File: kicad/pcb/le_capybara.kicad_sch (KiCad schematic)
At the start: 48 parts, among them J1 USB_C sink board 1.6mm, J2 OLED I2C, U2 STM32F072CBT6, U3 PRTR5V0U2X

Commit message: rerouted pcb
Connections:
- net APLEX_EN1: now also U2.3 (PC14); no longer U2.25 (PB12)
- net ROW0: now also U2.13 (PA3); no longer U2.18 (PB0)
- net ROW1: now also U2.15 (PA5); no longer U2.19 (PB1)
- net ROW2: now also U2.17 (PA7); no longer U2.20 (PB2)
- net ROW3: now also U2.19 (PB1); no longer U2.21 (PB10)
- no-connect marks 21 -> 18
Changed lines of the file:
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@@
   (no_connect (at 59.055 52.07))
   (no_connect (at 26.035 87.63))
-  (no_connect (at 59.055 44.45))
   (no_connect (at 26.035 54.61))
-  (no_connect (at 59.055 54.61))
+  (no_connect (at 26.035 95.25))
   (no_connect (at 59.055 59.69))
-  (no_connect (at 26.035 57.15))
-  (no_connect (at 59.055 49.53))
   (no_connect (at 60.325 69.85))
   (no_connect (at 59.055 36.83))
@@
     )
   )
+  (global_label "ROW1" (shape input) (at 59.055 49.53 0) (fields_autoplaced)
+    (effects (font (size 1.27 1.27)) (justify left))
+    (property "Intersheetrefs" "${INTERSHEET_REFS}" (at 67.2222 49.53 0)
+      (effects (font (size 1.27 1.27)) (justify left) hide)
+    )
+  )
   (global_label "BOOT0" (shape input) (at 83.82 83.82 0) (fields_autoplaced)
     (effects (font (size 1.27 1.27)) (justify left))
@@
     )
   )
-  (global_label "ROW2" (shape input) (at 26.035 69.85 180) (fields_autoplaced)
-    (effects (font (size 1.27 1.27)) (justify right))
-    (property "Intersheetrefs" "${INTERSHEET_REFS}" (at 17.8678 69.85 0)
+  (global_label "ROW3" (shape input) (at 26.035 67.31 180) (fields_autoplaced)
+    (effects (font (size 1.27 1.27)) (justify right))
+    (property "Intersheetrefs" "${INTERSHEET_REFS}" (at 17.8678 67.31 0)
       (effects (font (size 1.27 1.27)) (justify right) hide)
     )
@@
     )
   )
-  (global_label "ROW1" (shape input) (at 26.035 67.31 180) (fields_autoplaced)
-    (effects (font (size 1.27 1.27)) (justify right))
-    (property "Intersheetrefs" "${INTERSHEET_REFS}" (at 17.8678 67.31 0)
-      (effects (font (size 1.27 1.27)) (justify right) hide)
+  (global_label "ROW2" (shape input) (at 59.055 54.61 0) (fields_autoplaced)
+    (effects (font (size 1.27 1.27)) (justify left))
+    (property "Intersheetrefs" "${INTERSHEET_REFS}" (at 67.2222 54.61 0)
+      (effects (font (size 1.27 1.27)) (justify left) hide)
     )
   )
@@
     )
   )
-  (global_label "APLEX_EN1" (shape input) (at 26.035 95.25 180) (fields_autoplaced)
-    (effects (font (size 1.27 1.27)) (justify right))
-    (property "Intersheetrefs" "${INTERSHEET_REFS}" (at 12.7274 95.25 0)
-      (effects (font (size 1.27 1.27)) (justify right) hide)
-    )
-  )
-  (global_label "ROW0" (shape input) (at 26.035 64.77 180) (fields_autoplaced)
-    (effects (font (size 1.27 1.27)) (justify right))
-    (property "Intersheetrefs" "${INTERSHEET_REFS}" (at 17.8678 64.77 0)
-      (effects (font (size 1.27 1.27)) (justify right) hide)
+  (global_label "APLEX_EN1" (shape input) (at 26.035 57.15 180) (fields_autoplaced)
+    (effects (font (size 1.27 1.27)) (justify right))
+    (property "Intersheetrefs" "${INTERSHEET_REFS}" (at 12.7274 57.15 0)
+      (effects (font (size 1.27 1.27)) (justify right) hide)
+    )
+  )
+  (global_label "ROW0" (shape input) (at 59.055 44.45 0) (fields_autoplaced)
+    (effects (font (size 1.27 1.27)) (justify left))
+    (property "Intersheetrefs" "${INTERSHEET_REFS}" (at 67.2222 44.45 0)
+      (effects (font (size 1.27 1.27)) (justify left) hide)
     )
   )
@@
       (effects (font (size 1.27 1.27)) (justify right) hide)
     )
-  )
-  (global_label "ROW3" (shape input) (at 26.035 90.17 180) (fields_autoplaced)
-    (effects (font (size 1.27 1.27)) (justify right))
-    (property "Intersheetrefs" "${INTERSHEET_REFS}" (at 17.8678 90.17 0)
-      (effects (font (size 1.27 1.27)) (justify right) hide)
-    )

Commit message: getting ready for prototype
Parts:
- removed H1, H10, H11, H12, H13, H14, H15, H16, H17, H18, H19, H2, H20, H21, H22, H23, H24, H3, H4, H5, H6, H7, H8, H9: MountingHole, MountingHole:MountingHole_2.2mm_M2_DIN965, symbol Mechanical:MountingHole
- J1: value USB_C sink board 1.6mm -> USB_C sink board 1.3mm; LCSC C2936201 -> C3019717
- SW?: footprint modified_footrprints:SW_SPST_SKQG_WithoutStem -> modified_footprints:SW_SPST_SKQG_WithoutStem
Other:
- added sheet mounting_holes (mounting_holes.kicad_sch)

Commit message: getting ready for prototype
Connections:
- no-connect marks 18 -> 21
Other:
- moved on the sheet: C11, C8, C?, R?, SW?, U2

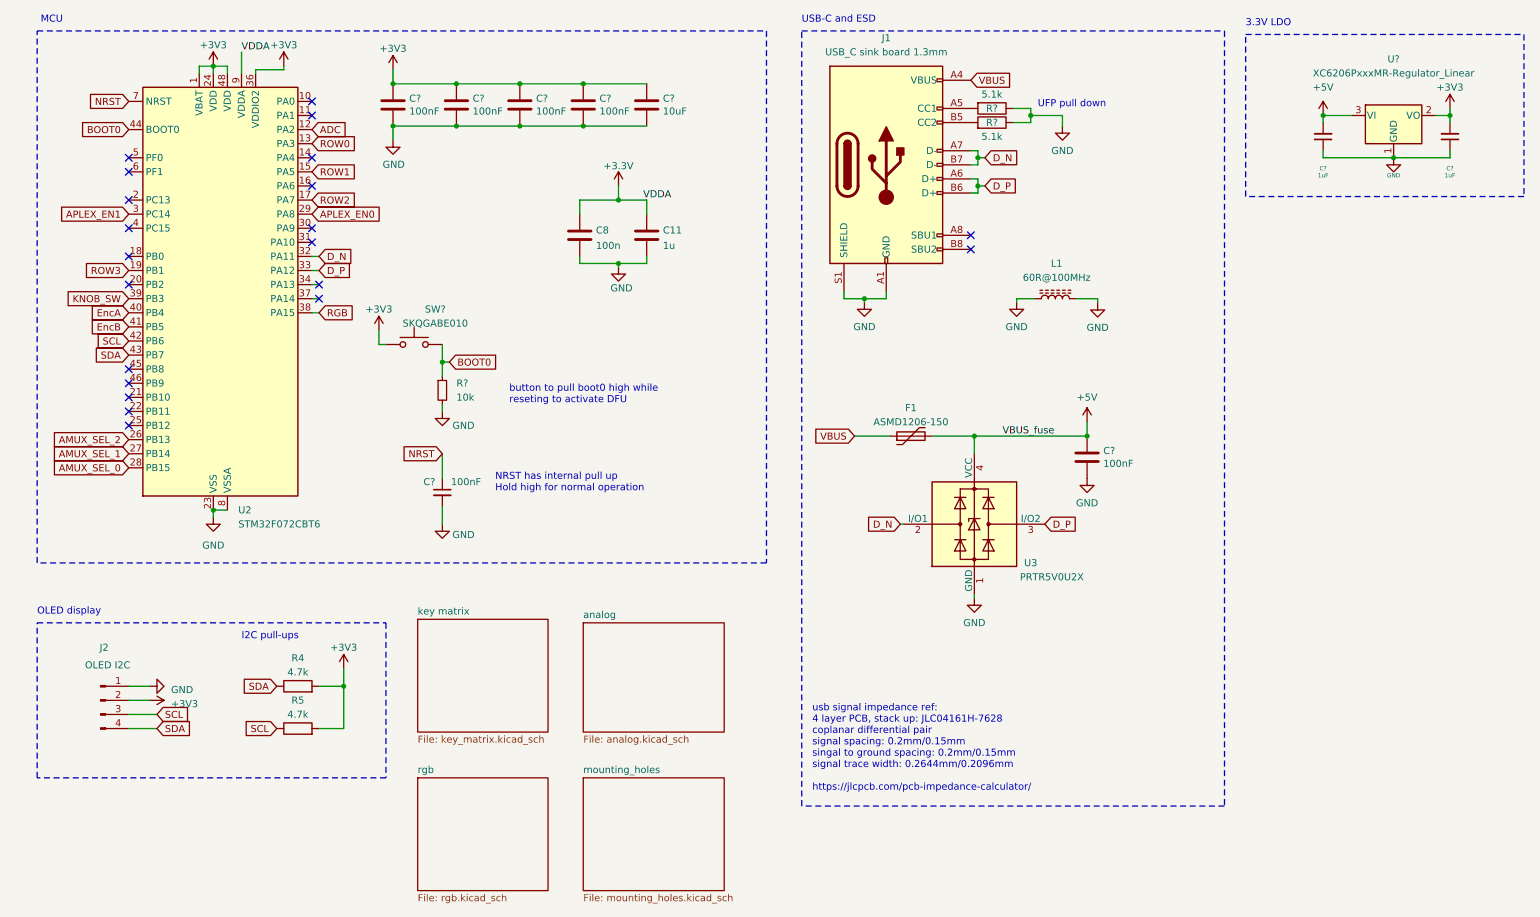
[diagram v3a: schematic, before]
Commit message: Major fixes after prototype order
Fixed the following:
- wrong RGB schematic, D106-D111 doesn't work
- discharge pin from analog circuit was not connected
- plate holes had the wrong diameter
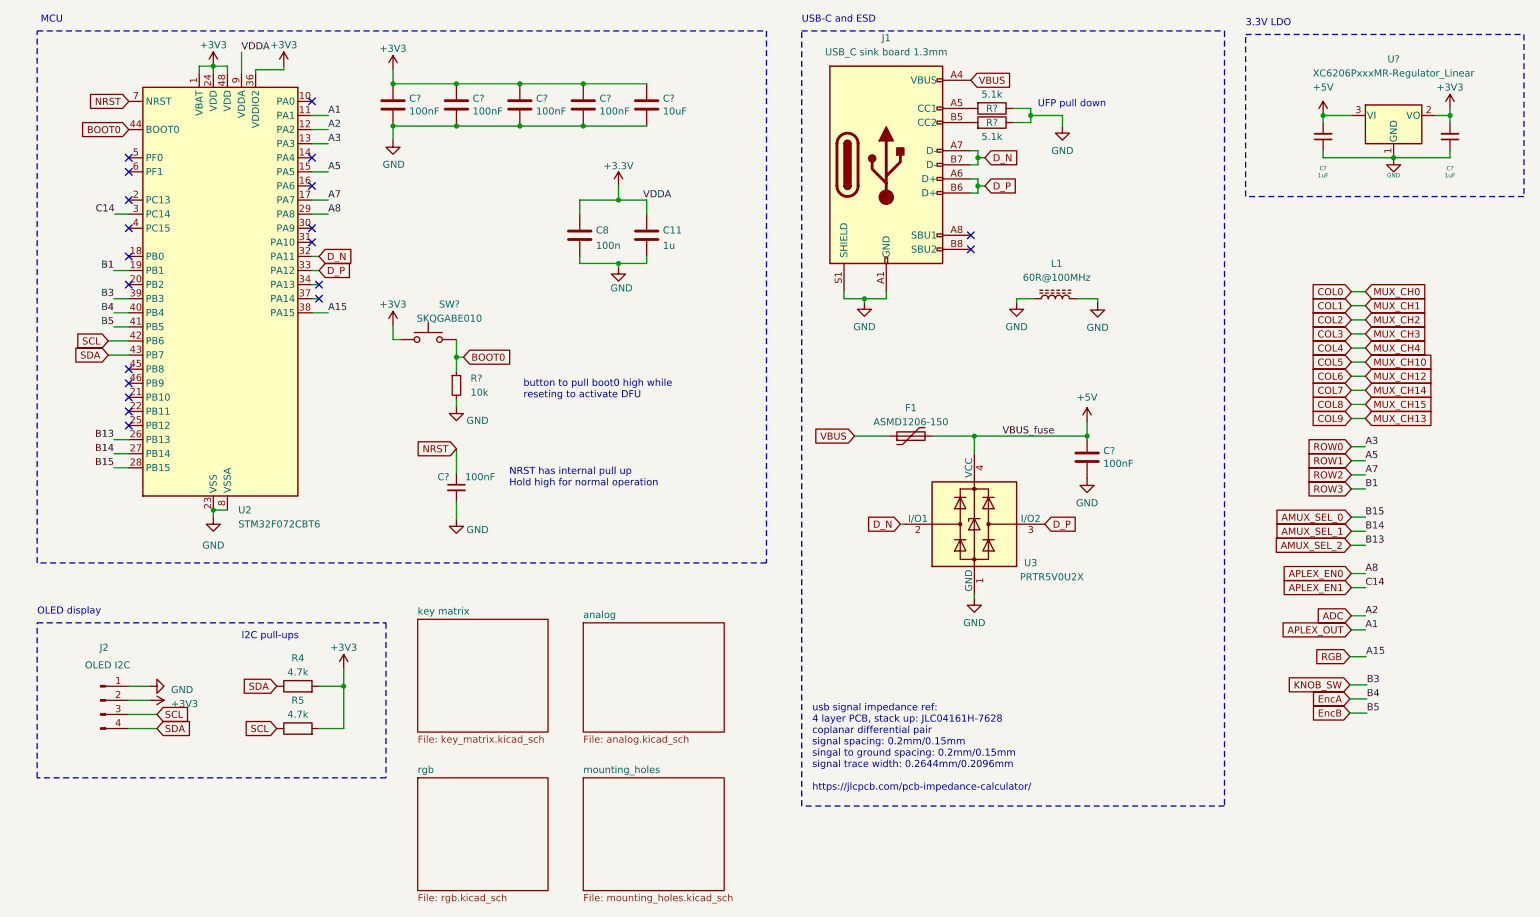
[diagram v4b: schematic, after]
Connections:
- net APLEX_OUT: now reaches U2.11 (PA1)
- no-connect marks 21 -> 20
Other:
- moved on the sheet: C?, R?, SW?
